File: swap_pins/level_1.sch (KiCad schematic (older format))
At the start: 6 parts, among them U201 PIC18F452-IP

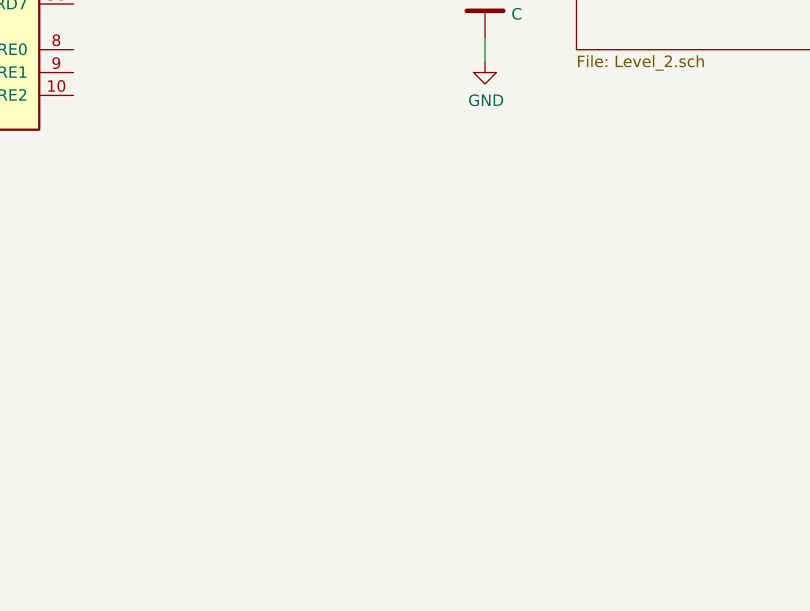
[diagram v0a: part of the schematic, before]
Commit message: added global label test
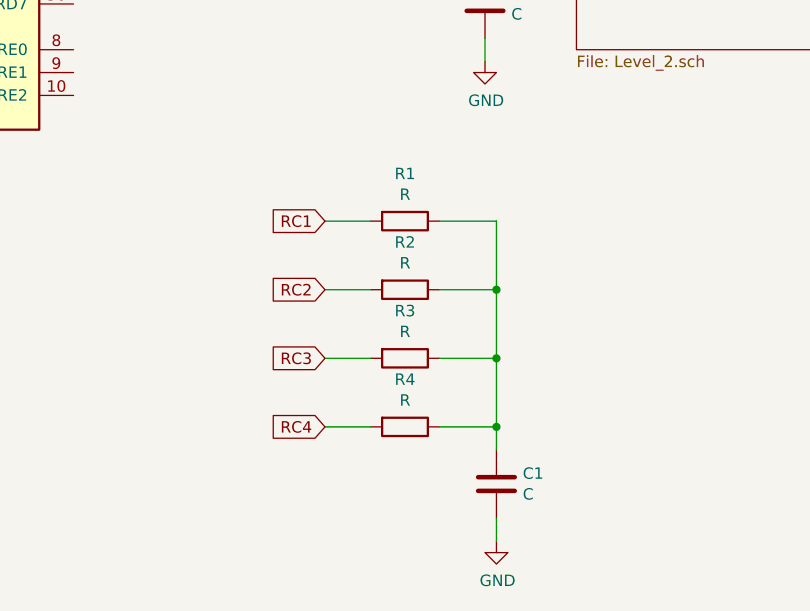
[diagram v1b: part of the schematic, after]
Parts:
- added C1: C, Capacitor_THT:C_Disc_D7.5mm_W5.0mm_P5.00mm, symbol Device:C
- added R1, R2, R3, R4: R, Resistor_THT:R_Axial_DIN0614_L14.3mm_D5.7mm_P20.32mm_Horizontal, symbol Device:R
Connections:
- net GND: now also C1.2
- new net: C1.1, R1.1, R2.1, R3.1, R4.1
- new net RC1: R1.2
- new net RC2: R2.2
- new net RC3: R3.2
- new net RC4: R4.2
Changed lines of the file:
@@
 EESchema Schematic File Version 4
+LIBS:swap_pins_test-cache
 EELAYER 26 0
 EELAYER END
@@
 Text Label 4100 3700 0    50   ~ 0
 RD4
+$Comp
+L Device:R R1
+U 1 1 5B2A0216
+P 5250 4950
+F 0 "R1" V 5043 4950 50  0000 C CNN
+F 1 "R" V 5134 4950 50  0000 C CNN
+F 2 "Resistor_THT:R_Axial_DIN0614_L14.3mm_D5.7mm_P20.32mm_Horizontal" V 5180 4950 50  0001 C CNN
+F 3 "~" H 5250 4950 50  0001 C CNN
+	1    5250 4950
+	0    1    1    0
+$EndComp
+$Comp
+L Device:R R2
+U 1 1 5B2A021D
+P 5250 5250
+F 0 "R2" V 5043 5250 50  0000 C CNN
+F 1 "R" V 5134 5250 50  0000 C CNN
+F 2 "Resistor_THT:R_Axial_DIN0614_L14.3mm_D5.7mm_P20.32mm_Horizontal" V 5180 5250 50  0001 C CNN
+F 3 "~" H 5250 5250 50  0001 C CNN
+	1    5250 5250
+	0    1    1    0
+$EndComp
+$Comp
+L Device:R R3
+U 1 1 5B2A0224
+P 5250 5550
+F 0 "R3" V 5043 5550 50  0000 C CNN
+F 1 "R" V 5134 5550 50  0000 C CNN
+F 2 "Resistor_THT:R_Axial_DIN0614_L14.3mm_D5.7mm_P20.32mm_Horizontal" V 5180 5550 50  0001 C CNN
+F 3 "~" H 5250 5550 50  0001 C CNN
+	1    5250 5550
+	0    1    1    0
+$EndComp
+$Comp
+L Device:R R4
+U 1 1 5B2A022B
+P 5250 5850
+F 0 "R4" V 5043 5850 50  0000 C CNN
+F 1 "R" V 5134 5850 50  0000 C CNN
+F 2 "Resistor_THT:R_Axial_DIN0614_L14.3mm_D5.7mm_P20.32mm_Horizontal" V 5180 5850 50  0001 C CNN
+F 3 "~" H 5250 5850 50  0001 C CNN
+	1    5250 5850
+	0    1    1    0
+$EndComp
+$Comp
+L Device:C C1
+U 1 1 5B2A0232
+P 5650 6100
+F 0 "C1" H 5765 6146 50  0000 L CNN
+F 1 "C" H 5765 6055 50  0000 L CNN
+F 2 "Capacitor_THT:C_Disc_D7.5mm_W5.0mm_P5.00mm" H 5688 5950 50  0001 C CNN
+F 3 "~" H 5650 6100 50  0001 C CNN
+	1    5650 6100
+	1    0    0    -1
+$EndComp
+Wire Wire Line
+	5100 4950 4900 4950
+Wire Wire Line
+	5100 5250 4900 5250
+Wire Wire Line
+	5100 5550 4900 5550
+Wire Wire Line
+	5100 5850 4900 5850
+Wire Wire Line
+	5400 5850 5650 5850
+Wire Wire Line
+	5650 5850 5650 5950
+Wire Wire Line
+	5400 5550 5650 5550
+Wire Wire Line
+	5650 5550 5650 5850
+Connection ~ 5650 5850
+Wire Wire Line
+	5400 5250 5650 5250
+Wire Wire Line
+	5650 5250 5650 5550
+Connection ~ 5650 5550
+Wire Wire Line
+	5400 4950 5650 4950
+Wire Wire Line
+	5650 4950 5650 5250
+Connection ~ 5650 5250
+$Comp
+L power:GND #PWR0104
+U 1 1 5B2A0248
+P 5650 6350
+F 0 "#PWR0104" H 5650 6100 50  0001 C CNN
+F 1 "GND" H 5655 6177 50  0000 C CNN
+F 2 "" H 5650 6350 50  0001 C CNN
+F 3 "" H 5650 6350 50  0001 C CNN
+	1    5650 6350
+	1    0    0    -1
+$EndComp
+Wire Wire Line
+	5650 6350 5650 6250
+Text GLabel 4900 4950 0    50   Input ~ 0
+RC1
+Text GLabel 4900 5250 0    50   Input ~ 0
+RC2
+Text GLabel 4900 5550 0    50   Input ~ 0
+RC3
+Text GLabel 4900 5850 0    50   Input ~ 0
+RC4
 $EndSCHEMATC

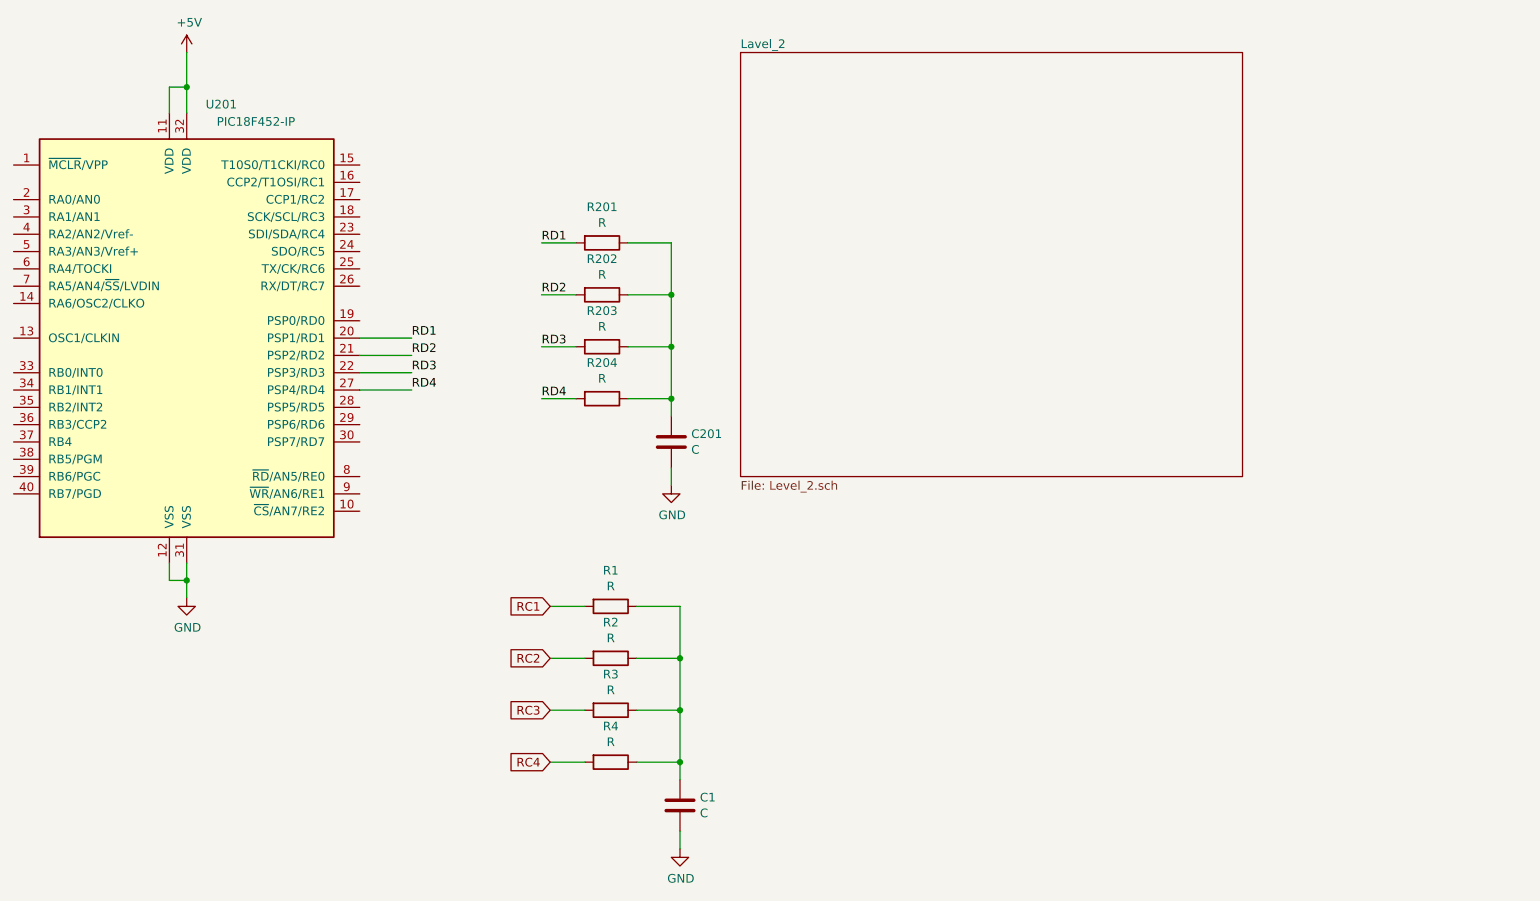
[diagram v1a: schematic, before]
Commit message: changed project to include hierarchical labels also
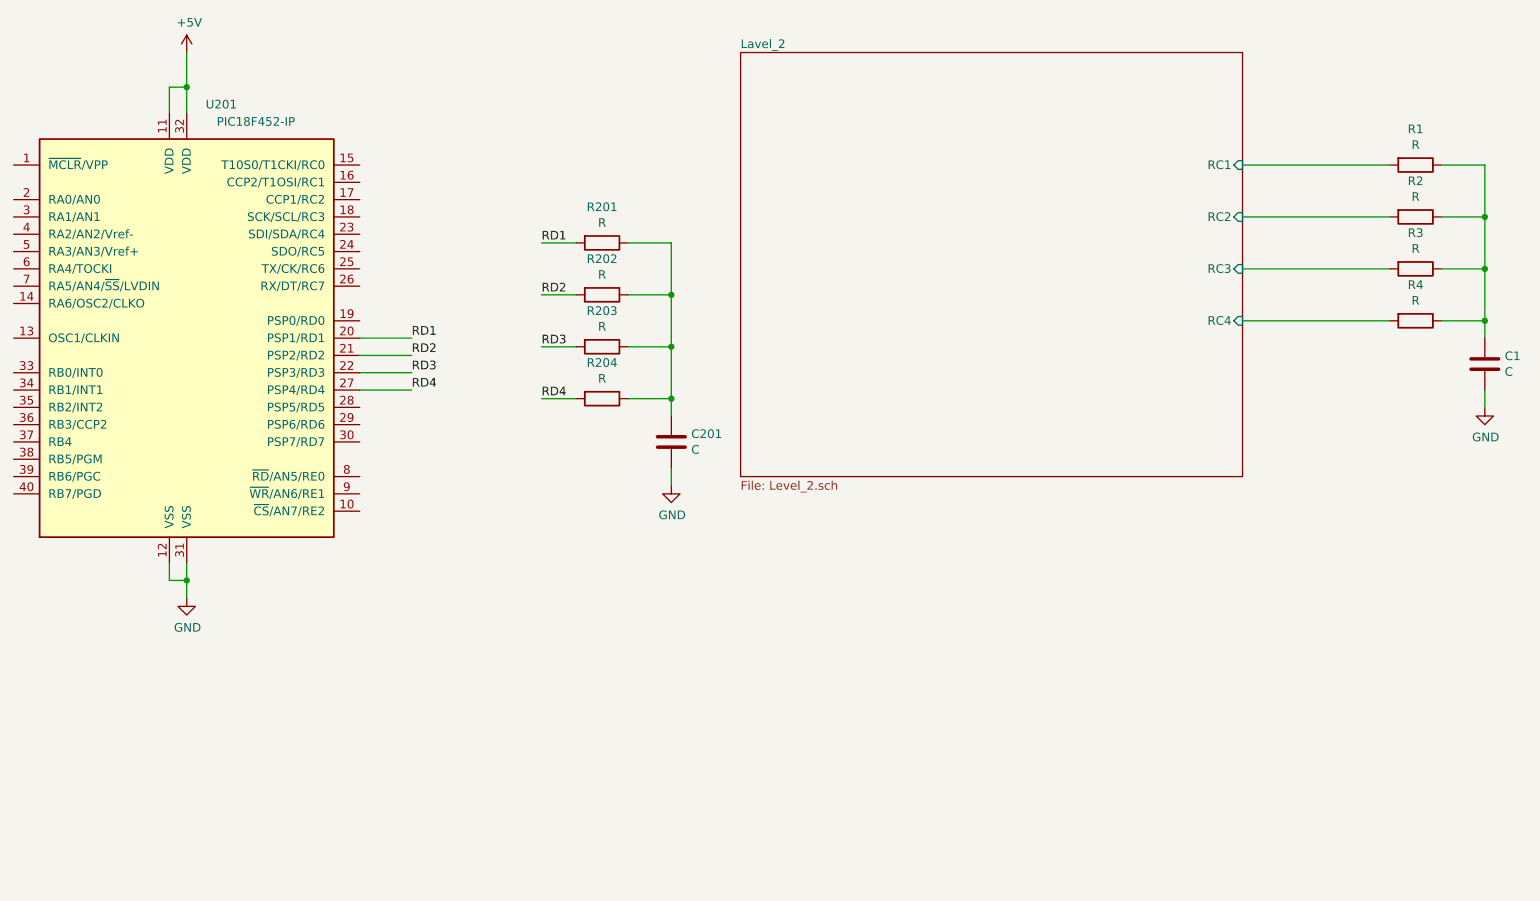
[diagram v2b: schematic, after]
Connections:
- net RC1 renamed Lavel_2/RC1
- net RC2 renamed Lavel_2/RC2
- net RC3 renamed Lavel_2/RC3
- net RC4 renamed Lavel_2/RC4
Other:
- moved on the sheet: C1, R1, R2, R3, R4
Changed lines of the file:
@@
 F0 "Lavel_2" 50
 F1 "Level_2.sch" 50
+F2 "RC1" I R 8900 2400 50
+F3 "RC2" I R 8900 2700 50
+F4 "RC3" I R 8900 3000 50
+F5 "RC4" I R 8900 3300 50
 $EndSheet
 $Comp
@@
 L Device:R R1
 U 1 1 5B2A0216
-P 5250 4950
-F 0 "R1" V 5043 4950 50  0000 C CNN
-F 1 "R" V 5134 4950 50  0000 C CNN
-F 2 "Resistor_THT:R_Axial_DIN0614_L14.3mm_D5.7mm_P20.32mm_Horizontal" V 5180 4950 50  0001 C CNN
-F 3 "~" H 5250 4950 50  0001 C CNN
-	1    5250 4950
+P 9900 2400
+F 0 "R1" V 9693 2400 50  0000 C CNN
+F 1 "R" V 9784 2400 50  0000 C CNN
+F 2 "Resistor_THT:R_Axial_DIN0614_L14.3mm_D5.7mm_P20.32mm_Horizontal" V 9830 2400 50  0001 C CNN
+F 3 "~" H 9900 2400 50  0001 C CNN
+	1    9900 2400
 	0    1    1    0
 $EndComp
@@
 L Device:R R2
 U 1 1 5B2A021D
-P 5250 5250
-F 0 "R2" V 5043 5250 50  0000 C CNN
-F 1 "R" V 5134 5250 50  0000 C CNN
-F 2 "Resistor_THT:R_Axial_DIN0614_L14.3mm_D5.7mm_P20.32mm_Horizontal" V 5180 5250 50  0001 C CNN
-F 3 "~" H 5250 5250 50  0001 C CNN
-	1    5250 5250
+P 9900 2700
+F 0 "R2" V 9693 2700 50  0000 C CNN
+F 1 "R" V 9784 2700 50  0000 C CNN
+F 2 "Resistor_THT:R_Axial_DIN0614_L14.3mm_D5.7mm_P20.32mm_Horizontal" V 9830 2700 50  0001 C CNN
+F 3 "~" H 9900 2700 50  0001 C CNN
+	1    9900 2700
 	0    1    1    0
 $EndComp
@@
 L Device:R R3
 U 1 1 5B2A0224
-P 5250 5550
-F 0 "R3" V 5043 5550 50  0000 C CNN
-F 1 "R" V 5134 5550 50  0000 C CNN
-F 2 "Resistor_THT:R_Axial_DIN0614_L14.3mm_D5.7mm_P20.32mm_Horizontal" V 5180 5550 50  0001 C CNN
-F 3 "~" H 5250 5550 50  0001 C CNN
-	1    5250 5550
+P 9900 3000
+F 0 "R3" V 9693 3000 50  0000 C CNN
+F 1 "R" V 9784 3000 50  0000 C CNN
+F 2 "Resistor_THT:R_Axial_DIN0614_L14.3mm_D5.7mm_P20.32mm_Horizontal" V 9830 3000 50  0001 C CNN
+F 3 "~" H 9900 3000 50  0001 C CNN
+	1    9900 3000
 	0    1    1    0
 $EndComp
@@
 L Device:R R4
 U 1 1 5B2A022B
-P 5250 5850
-F 0 "R4" V 5043 5850 50  0000 C CNN
-F 1 "R" V 5134 5850 50  0000 C CNN
-F 2 "Resistor_THT:R_Axial_DIN0614_L14.3mm_D5.7mm_P20.32mm_Horizontal" V 5180 5850 50  0001 C CNN
-F 3 "~" H 5250 5850 50  0001 C CNN
-	1    5250 5850
+P 9900 3300
+F 0 "R4" V 9693 3300 50  0000 C CNN
+F 1 "R" V 9784 3300 50  0000 C CNN
+F 2 "Resistor_THT:R_Axial_DIN0614_L14.3mm_D5.7mm_P20.32mm_Horizontal" V 9830 3300 50  0001 C CNN
+F 3 "~" H 9900 3300 50  0001 C CNN
+	1    9900 3300
 	0    1    1    0
 $EndComp
@@
 L Device:C C1
 U 1 1 5B2A0232
-P 5650 6100
-F 0 "C1" H 5765 6146 50  0000 L CNN
-F 1 "C" H 5765 6055 50  0000 L CNN
-F 2 "Capacitor_THT:C_Disc_D7.5mm_W5.0mm_P5.00mm" H 5688 5950 50  0001 C CNN
-F 3 "~" H 5650 6100 50  0001 C CNN
-	1    5650 6100
-	1    0    0    -1
-$EndComp
-Wire Wire Line
-	5100 4950 4900 4950
-Wire Wire Line
-	5100 5250 4900 5250
-Wire Wire Line
-	5100 5550 4900 5550
-Wire Wire Line
-	5100 5850 4900 5850
-Wire Wire Line
-	5400 5850 5650 5850
-Wire Wire Line
-	5650 5850 5650 5950
-Wire Wire Line
-	5400 5550 5650 5550
-Wire Wire Line
-	5650 5550 5650 5850
-Connection ~ 5650 5850
-Wire Wire Line
-	5400 5250 5650 5250
-Wire Wire Line
-	5650 5250 5650 5550
-Connection ~ 5650 5550
-Wire Wire Line
-	5400 4950 5650 4950
-Wire Wire Line
-	5650 4950 5650 5250
-Connection ~ 5650 5250
+P 10300 3550
+F 0 "C1" H 10415 3596 50  0000 L CNN
+F 1 "C" H 10415 3505 50  0000 L CNN
+F 2 "Capacitor_THT:C_Disc_D7.5mm_W5.0mm_P5.00mm" H 10338 3400 50  0001 C CNN
+F 3 "~" H 10300 3550 50  0001 C CNN
+	1    10300 3550
+	1    0    0    -1
+$EndComp
+Wire Wire Line
+	10050 3300 10300 3300
+Wire Wire Line
+	10300 3300 10300 3400
+Wire Wire Line
+	10050 3000 10300 3000
+Wire Wire Line
+	10300 3000 10300 3300
+Connection ~ 10300 3300
+Wire Wire Line
+	10050 2700 10300 2700
+Wire Wire Line
+	10300 2700 10300 3000
+Connection ~ 10300 3000
+Wire Wire Line
+	10050 2400 10300 2400
+Wire Wire Line
+	10300 2400 10300 2700
+Connection ~ 10300 2700
 $Comp
 L power:GND #PWR0104
 U 1 1 5B2A0248
-P 5650 6350
-F 0 "#PWR0104" H 5650 6100 50  0001 C CNN
-F 1 "GND" H 5655 6177 50  0000 C CNN
-F 2 "" H 5650 6350 50  0001 C CNN
-F 3 "" H 5650 6350 50  0001 C CNN
-	1    5650 6350
-	1    0    0    -1
-$EndComp
-Wire Wire Line
-	5650 6350 5650 6250
-Text GLabel 4900 4950 0    50   Input ~ 0
-RC1
-Text GLabel 4900 5250 0    50   Input ~ 0
-RC2
-Text GLabel 4900 5550 0    50   Input ~ 0
-RC3
-Text GLabel 4900 5850 0    50   Input ~ 0
-RC4
+P 10300 3800
+F 0 "#PWR0104" H 10300 3550 50  0001 C CNN
+F 1 "GND" H 10305 3627 50  0000 C CNN
+F 2 "" H 10300 3800 50  0001 C CNN
+F 3 "" H 10300 3800 50  0001 C CNN
+	1    10300 3800
+	1    0    0    -1
+$EndComp
+Wire Wire Line
+	10300 3800 10300 3700
+Wire Wire Line
+	8900 2400 9750 2400
+Wire Wire Line
+	8900 2700 9750 2700
+Wire Wire Line
+	8900 3000 9750 3000
+Wire Wire Line
+	8900 3300 9750 3300
 $EndSCHEMATC

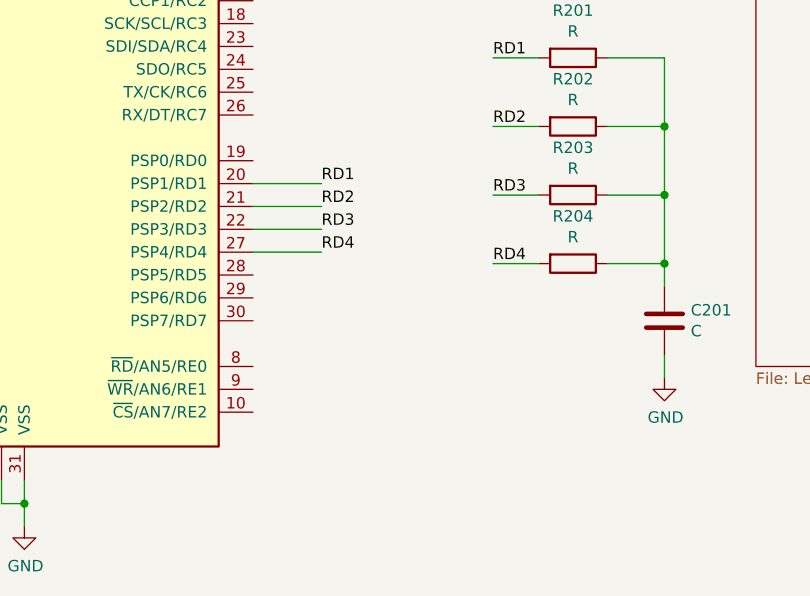
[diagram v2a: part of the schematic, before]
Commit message: Overwritten the plugin with V2 version
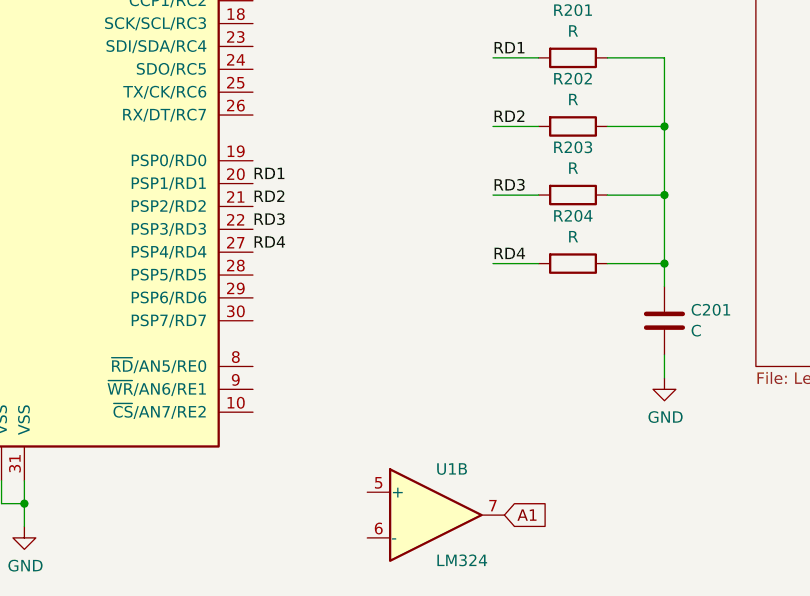
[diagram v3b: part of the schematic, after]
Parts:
- added U1: LM324, symbol Amplifier_Operational:LM324
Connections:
- new net A1: U1.7
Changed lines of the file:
@@
 	1    0    0    -1
 $EndComp
-Wire Wire Line
-	3800 3400 4100 3400
-Wire Wire Line
-	3800 3500 4100 3500
-Wire Wire Line
-	3800 3600 4100 3600
-Wire Wire Line
-	3800 3700 4100 3700
-Text Label 4100 3400 0    50   ~ 0
+Text Label 3800 3400 0    50   ~ 0
 RD1
-Text Label 4100 3500 0    50   ~ 0
+Text Label 3800 3500 0    50   ~ 0
 RD2
-Text Label 4100 3600 0    50   ~ 0
+Text Label 3800 3600 0    50   ~ 0
 RD3
-Text Label 4100 3700 0    50   ~ 0
+Text Label 3800 3700 0    50   ~ 0
 RD4
 $Comp
@@
 Wire Wire Line
 	8900 3300 9750 3300
+Text GLabel 4900 4850 2    50   Input ~ 0
+A1
+$Comp
+L Amplifier_Operational:LM324 U1
+U 2 1 5B34B8B0
+P 4600 4850
+F 0 "U1" H 4600 5050 50  0000 L CNN
+F 1 "LM324" H 4600 4650 50  0000 L CNN
+F 2 "" H 4550 4950 50  0001 C CNN
+F 3 "http://www.ti.com/lit/ds/symlink/lm2902-n.pdf" H 4650 5050 50  0001 C CNN
+	2    4600 4850
+	1    0    0    -1
+$EndComp
 $EndSCHEMATC
